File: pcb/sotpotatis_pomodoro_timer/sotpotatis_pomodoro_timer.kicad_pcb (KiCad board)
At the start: 4 copper layers, 85 x 68.2 mm, 58 parts, among them J1 GENERIC_PWR_IN, J2 USB_C_PWR_IN, SW1 RIGHT_BTN, SW2 PRESET_1_BTN, SW3 PRESET_2_BTN, SW4 PRESET_3_BTN, SW5 LEFT_BTN, SW6 PWR_SWITCH, U1 ATtiny84A-P

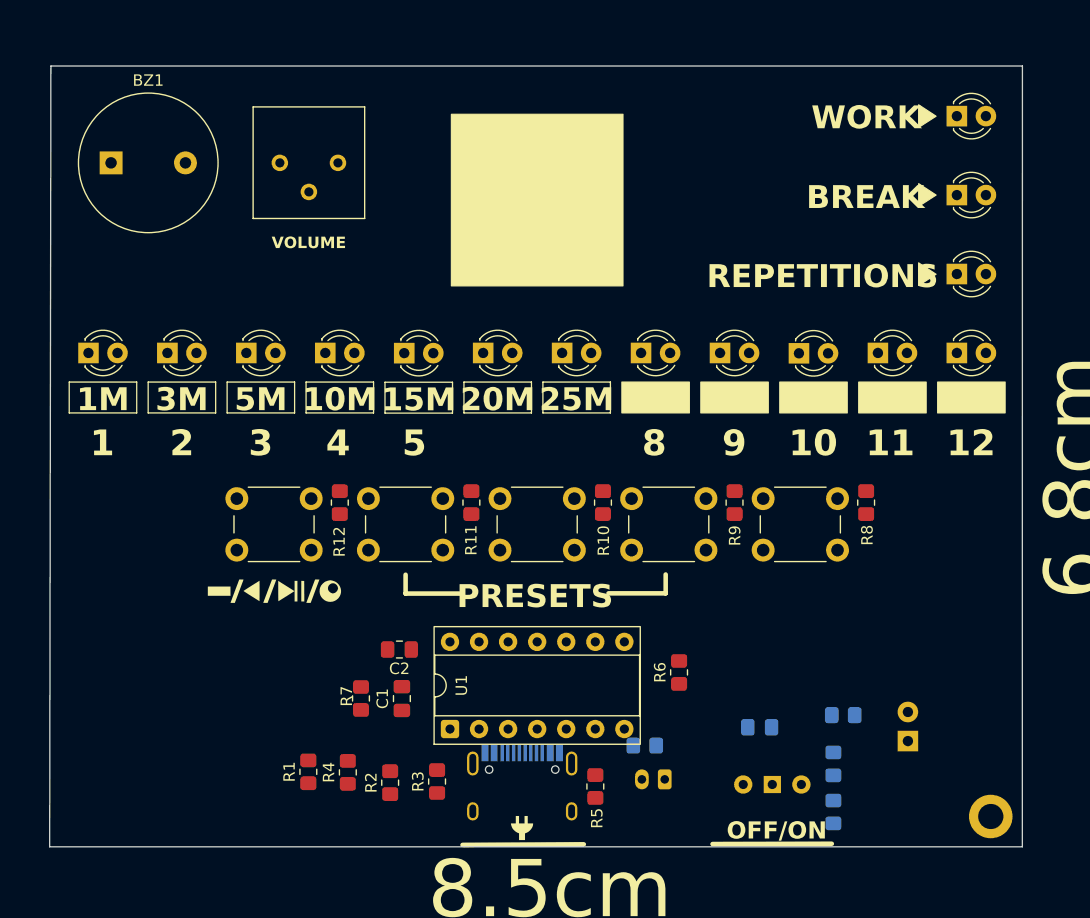
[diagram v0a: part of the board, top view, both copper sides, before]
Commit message: add: Update component placement (primarily switch+LED centering) of PCB variant 1
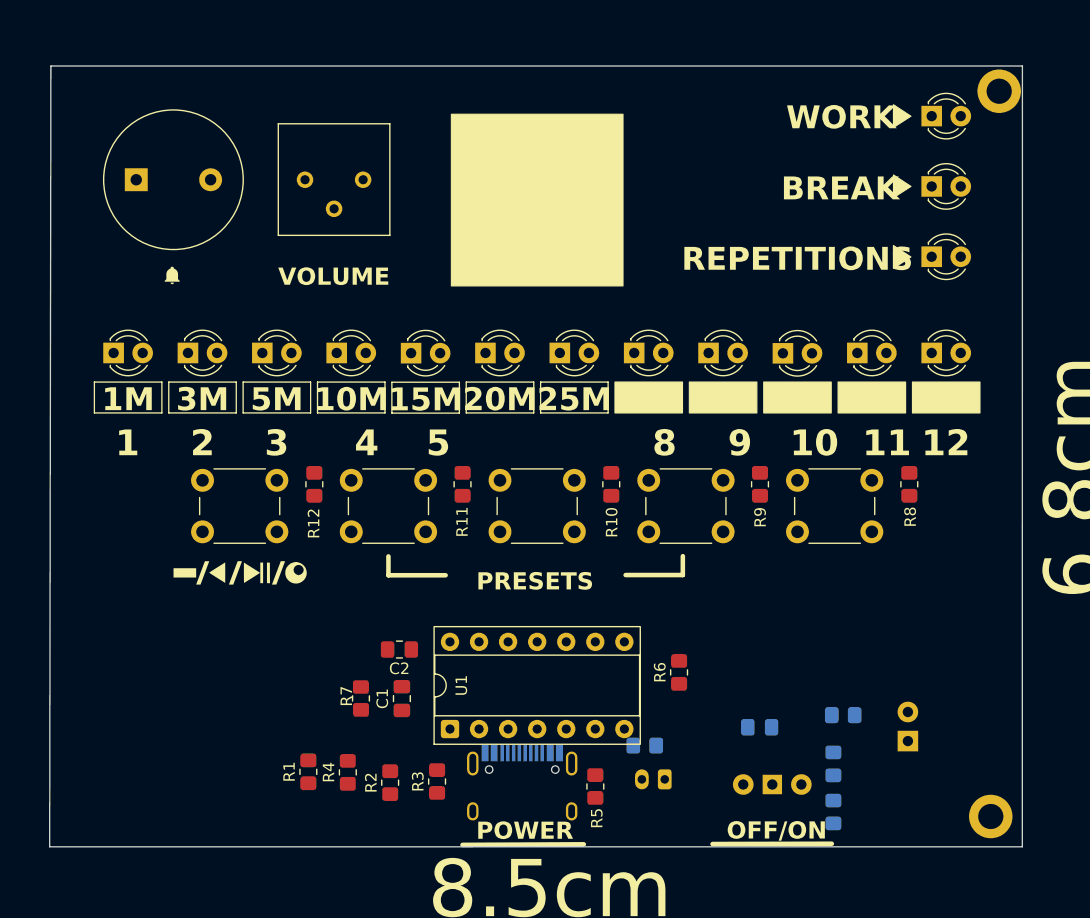
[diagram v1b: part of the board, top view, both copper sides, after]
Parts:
- added REF**: MountingHole_2.2mm_M2_DIN965_Pad, MountingHole:MountingHole_2.2mm_M2_DIN965_Pad, F.Cu at (172.4, 51.6)
- moved G*** 57.0 mm to (100.2, 67.6)
- moved R8 4.10 mm to (164.6, 85.9)
- moved SW1 3.40 mm to (154.8, 85.6)
- moved SW5 3.40 mm to (102.8, 85.6)
- moved G*** 3.40 mm to (106.1, 93.7)
- moved R12 2.74 mm to (112.6, 85.9)
- moved R9 2.74 mm to (151.5, 85.9)
- moved D15 2.67 mm to (166.5, 66.0)
- moved BZ1 2.65 mm to (97.8, 59.3)
- moved RV1 2.65 mm to (111.8, 59.3)
- moved D14 2.33 mm to (166.5, 59.9)
- moved D1 2.20 mm to (95.0, 74.4)
- moved D12 2.20 mm to (166.5, 74.4)
- moved D13 2.20 mm to (166.5, 53.7)
- moved SW2 2.19 mm to (141.8, 85.6)
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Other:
- board text added: "POWER"

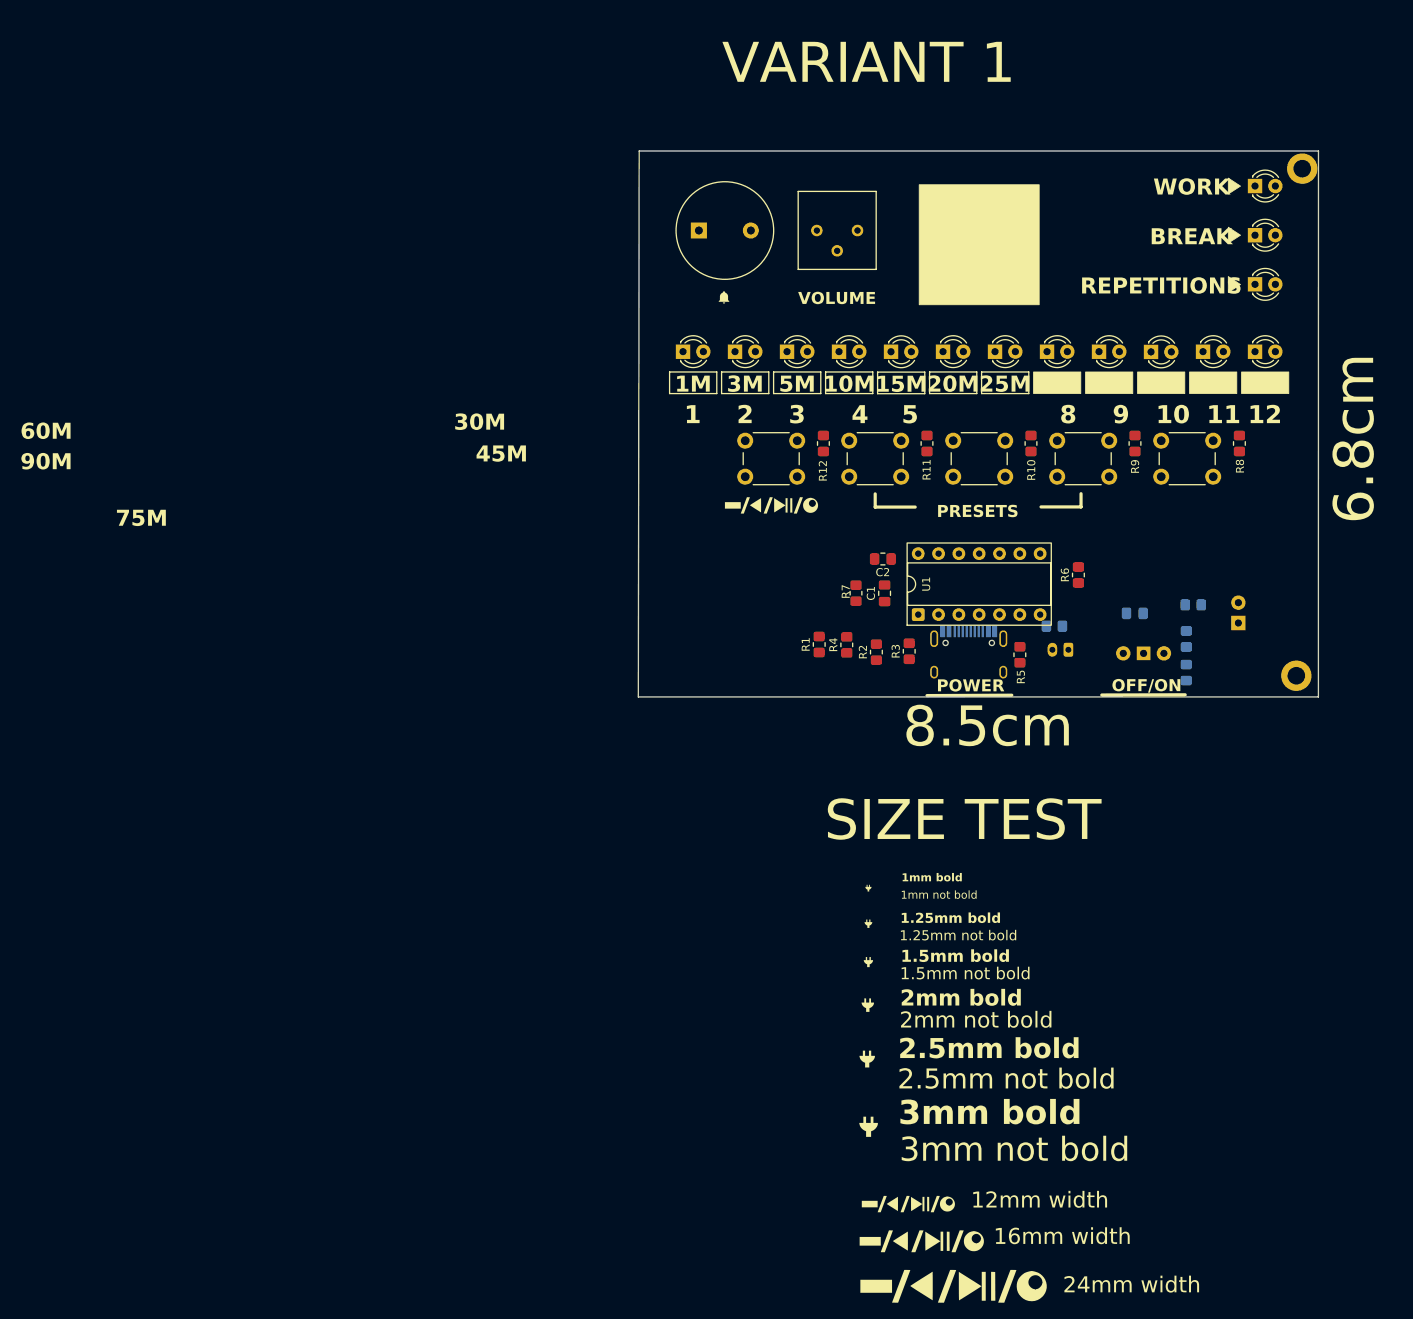
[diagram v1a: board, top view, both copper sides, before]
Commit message: add: Final component placement (except SMD) for PCB
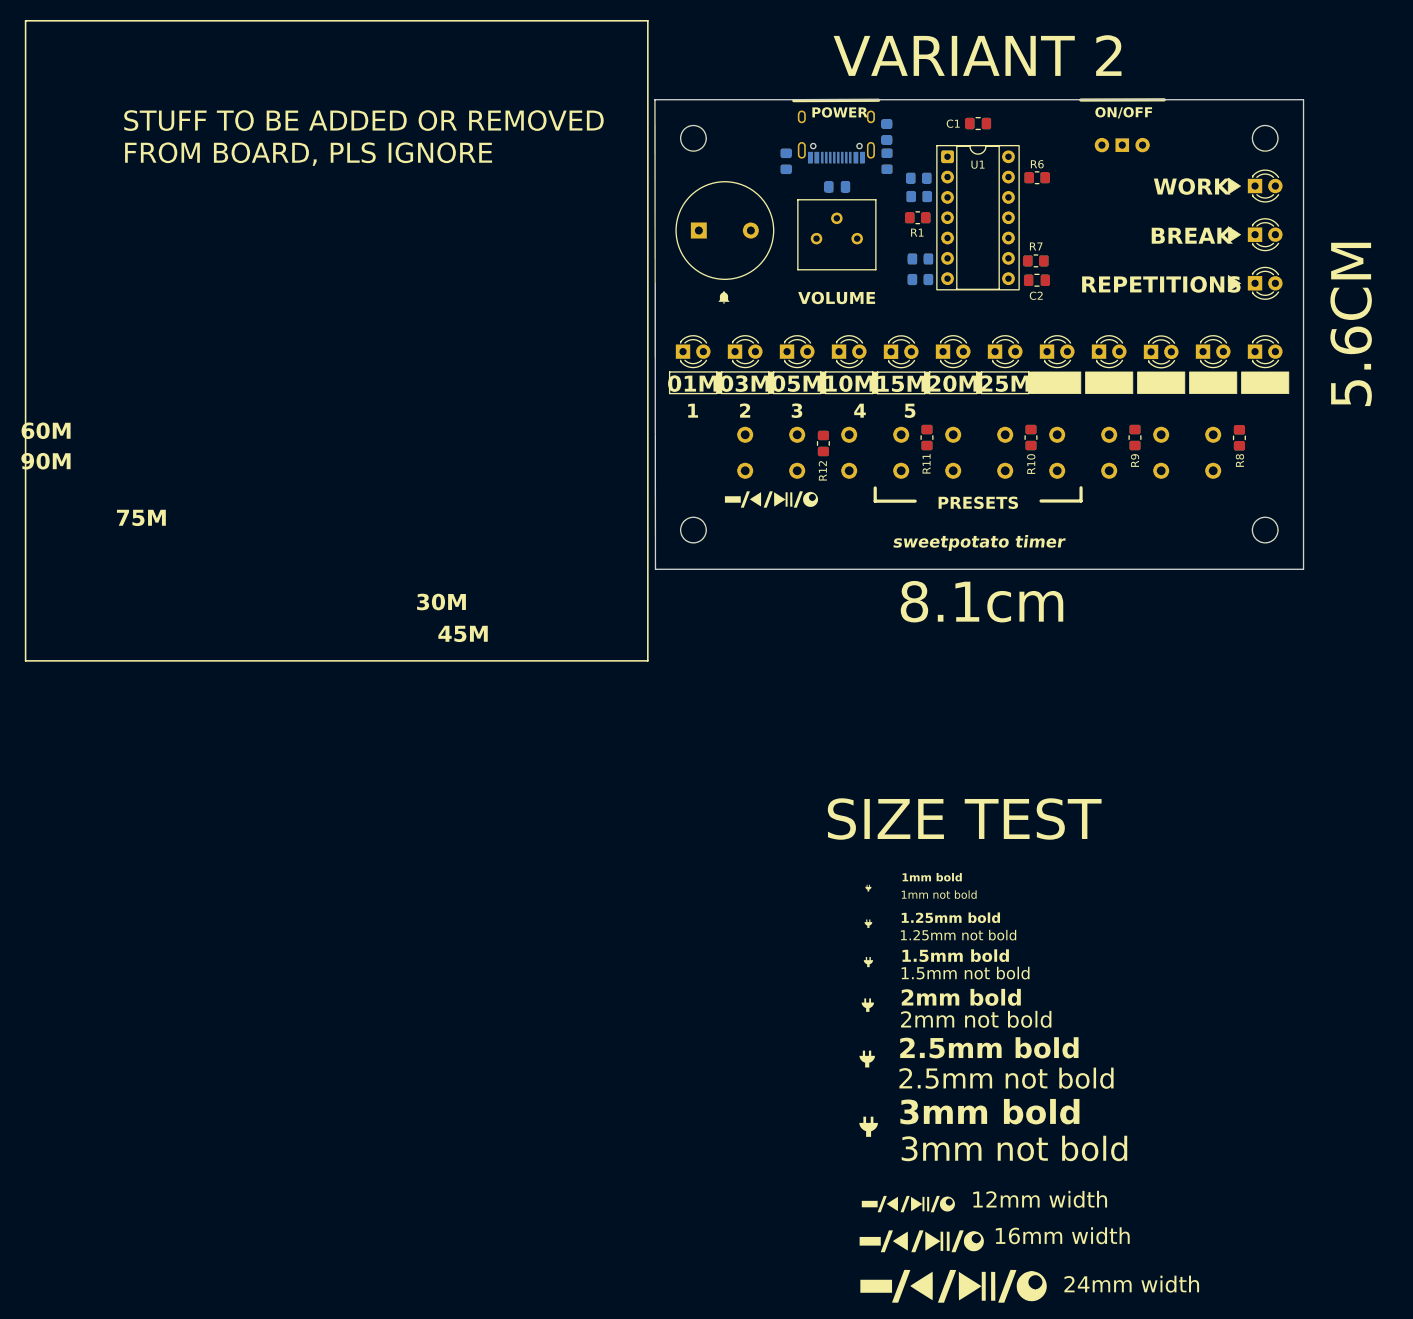
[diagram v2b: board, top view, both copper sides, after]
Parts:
- removed D16: LED, LED_THT:LED_D3.0mm
- removed J1: GENERIC_PWR_IN, Connector_JST:JST_PH_S2B-PH-K_1x02_P2.00mm_Horizontal
- removed R13: 2.2k, Resistor_SMD:R_0805_2012Metric_Pad1.20x1.40mm_HandSolder
- removed the REF** at (172.4, 51.6)
- removed the REF** at (171.7, 115.0)
- added REF**: MountingHole_3.2mm_M3, MountingHole:MountingHole_3.2mm_M3, F.Cu at (96.3, 47.8)
- added REF**: MountingHole_3.2mm_M3, MountingHole:MountingHole_3.2mm_M3, F.Cu at (167.8, 47.8)
- added REF**: MountingHole_3.2mm_M3, MountingHole:MountingHole_3.2mm_M3, F.Cu at (96.3, 96.8)
- added REF**: MountingHole_3.2mm_M3, MountingHole:MountingHole_3.2mm_M3, F.Cu at (167.8, 96.8)
- R2, R3, R4, R5: moved to B.Cu
- RV1: footprint Potentiometer_THT:Potentiometer_Bourns_3386P_Vertical -> custom-project-libraries:Potentiometer_Bourns_3386P_Vertical
- SW1: renamed from SW5; footprint Button_Switch_THT:SW_PUSH_6mm_H5mm -> custom-project-libraries:SW_PUSH_6mm_H5mm
- SW2: renamed from SW4; value PRESET_3_BTN -> PRESET_1_BTN; footprint Button_Switch_THT:SW_PUSH_6mm_H5mm -> custom-project-libraries:SW_PUSH_6mm_H5mm
- SW3: footprint Button_Switch_THT:SW_PUSH_6mm_H5mm -> custom-project-libraries:SW_PUSH_6mm_H5mm
- SW4: renamed from SW2; value PRESET_1_BTN -> PRESET_3_BTN; footprint Button_Switch_THT:SW_PUSH_6mm_H5mm -> custom-project-libraries:SW_PUSH_6mm_H5mm
- SW5: renamed from SW1; footprint Button_Switch_THT:SW_PUSH_6mm_H5mm -> custom-project-libraries:SW_PUSH_6mm_H5mm
- moved R14 77.9 mm to (107.9, 50.6), turned to -90 degrees
- moved R16 77.2 mm to (120.5, 47.0), turned to -90 degrees
- moved J2 69.3 mm to (114.2, 46.1), turned to 0 degrees
- moved C3 65.0 mm to (114.3, 53.9)
- moved SW6 63.6 mm to (149.9, 48.6), turned to 0 degrees
- moved R15 61.8 mm to (120.5, 50.6), turned to -90 degrees
- moved C1 59.9 mm to (131.9, 45.9), turned to 0 degrees
- moved R2 59.5 mm to (124.5, 52.8), turned to 0 degrees
- moved U1 57.3 mm to (128.1, 50.1), turned to 0 degrees
- moved R3 56.9 mm to (124.5, 55.1), turned to 0 degrees
- moved R1 54.7 mm to (124.4, 57.7), turned to 180 degrees
- moved R6 49.9 mm to (139.3, 52.7), turned to 0 degrees
- moved R4 49.1 mm to (124.7, 62.9), turned to 0 degrees
- moved R5 48.5 mm to (124.7, 65.4), turned to 0 degrees
- moved R7 47.2 mm to (139.1, 63.1), turned to 180 degrees
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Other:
- board size 85 x 68.2 mm -> 81.1 x 58.7 mm
- board text added: "01M"
- board text added: "03M"
- board text added: "05M"
- board text added: "5.6CM"
- board text added: "8.1cm"
- board text added: "ON/OFF"
- board text added: "STUFF TO BE ADDED OR REMOVED FROM BOARD, PLS IGNORE"
- board text added: "VARIANT 2"
- board text added: "sweetpotato timer"
- board text removed: "10"
- board text removed: "11"
- board text removed: "12"
- board text removed: "1M"
- board text removed: "3M"
- board text removed: "5M"
- board text removed: "6.8cm"
- board text removed: "8"
- board text removed: "8.5cm"
- board text removed: "9"
- board text removed: "OFF/ON"
- board text removed: "VARIANT 1"
